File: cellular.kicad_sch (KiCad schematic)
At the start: 37 parts, among them J2 USB_C_Receptacle_USB2.0_14P, J4 SIM_Card_Shielded, J6 Conn_01x04_Pin, Q2 MMBT3904, Q3 MMBT3904, Q4 MMBT3904, SW4 SW_Push, U13 SIM7080G, U19 TPD3F303DPV

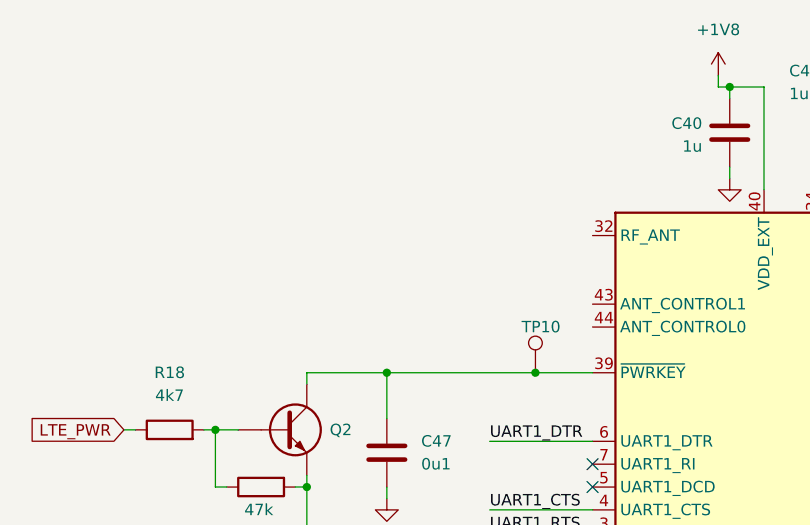
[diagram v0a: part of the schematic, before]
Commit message: schem: add modem lte rf ant
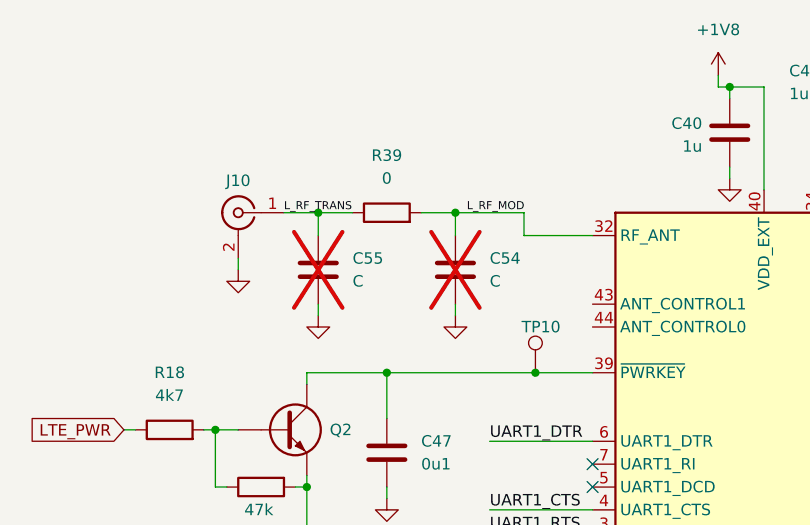
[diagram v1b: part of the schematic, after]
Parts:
- added C54, C55: C, Capacitor_SMD:C_0402_1005Metric, symbol Device:C
- added J10: Conn_Coaxial, Connector_Coaxial:U.FL_Hirose_U.FL-R-SMT-1_Vertical, symbol Connector:Conn_Coaxial
- added R39: 0, symbol Device:R
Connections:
- net GND: now also C54.2, C55.2, J10.2 (Ext)
- net L_RF_MOD: now reaches U13.32 (RF_ANT)
- net L_RF_MOD: now also C54.1, R39.2
- new net L_RF_TRANS: C55.1, J10.1 (In), R39.1

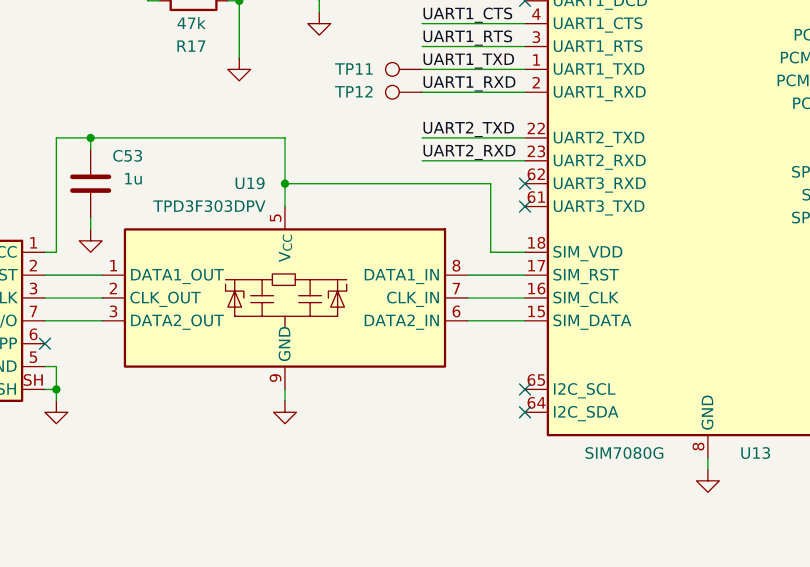
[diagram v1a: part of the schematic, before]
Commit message: schem: add test points
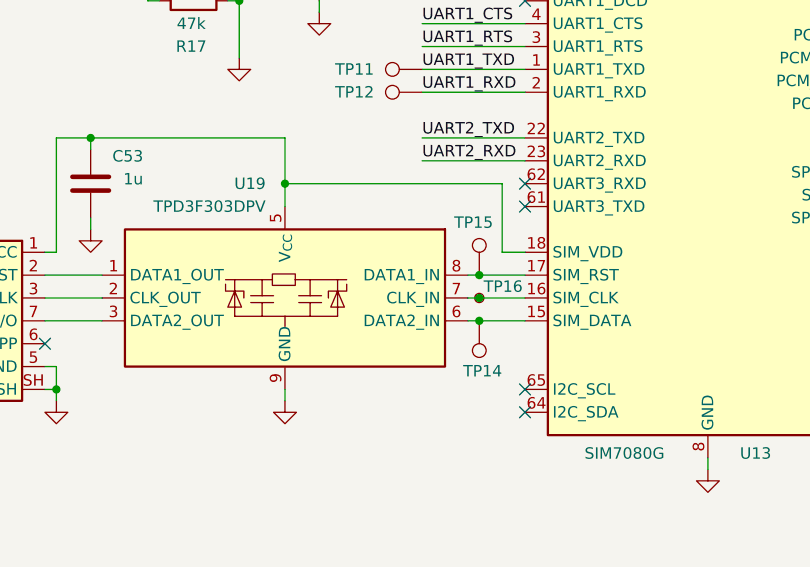
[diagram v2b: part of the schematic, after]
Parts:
- added TP14, TP15: TestPoint, TestPoint:TestPoint_Pad_D2.0mm, symbol Connector:TestPoint
- added TP16: TestPoint, TestPoint:TestPoint_Pad_D2.0mm, symbol Connector:TestPoint_Small
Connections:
- net at U13.15 (SIM_DATA), U19.6 (DATA2_IN): now also TP14.1
- net at U13.16 (SIM_CLK), U19.7 (CLK_IN): now also TP16.1
- net at U13.17 (SIM_RST), U19.8 (DATA1_IN): now also TP15.1

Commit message: schem: run and fix ERC
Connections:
- net D+ renamed MODEM_D+
- net D- renamed MODEM_D-
- no-connect marks 21 -> 24
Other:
- moved on the sheet: SW4

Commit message: schem: add net classes
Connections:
- net L_RF_MOD renamed RF_MOD_L
- net L_RF_TRANS renamed RF_TRANS_L
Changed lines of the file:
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@@
 		)
 	)
-	(label "L_RF_MOD"
+	(label "RF_MOD_L"
 		(at 196.85 38.1 0)
 		(effects
@@
 		)
 	)
-	(label "L_RF_TRANS"
+	(label "RF_TRANS_L"
 		(at 176.53 38.1 0)
 		(effects
@@
 		)
 	)
+	(rule_area
+		(exclude_from_sim no)
+		(in_bom yes)
+		(on_board yes)
+		(dnp no)
+		(polyline
+			(pts
+				(xy 127 91.44) (xy 127 121.285) (xy 207.01 121.285) (xy 207.01 91.44)
+			)
+			(stroke
+				(width 0)
+				(type dash)
+			)
+			(fill
+				(type none)
+			)
+		)
+	)
+	(netclass_flag ""
+		(length 2.54)
+		(shape round)
+		(at 129.54 91.44 0)
+		(fields_autoplaced yes)
+		(effects
+			(font
+				(size 1.27 1.27)
+			)
+			(justify left bottom)
+		)
+		(property "Netclass" "SIM"
+			(at 130.2385 88.9 0)
+			(show_name no)
+			(do_not_autoplace no)
+			(effects
+				(font
+					(size 1.27 1.27)
+				)
+				(justify left)
+			)
+		)
+		(property "Component Class" ""
+			(at -102.87 3.81 0)
+			(show_name no)
+			(do_not_autoplace no)
+			(effects
+				(font
+					(size 1.27 1.27)
+					(italic yes)
+				)
+			)
+		)
+	)
 	(symbol
 		(lib_id "power:GND")
@@
 		(dnp no)
 		(property "Reference" "TP14"
-			(at 208.28 109.728 0)
+			(at 206.502 110.49 0)
 			(show_name no)
 			(do_not_autoplace no)
@@
 		(dnp no)
 		(property "Reference" "U19"
-			(at 182.0067 88.9 0)
+			(at 180.594 110.998 0)
 			(show_name no)
 			(do_not_autoplace no)
@@
 		)
 		(property "Value" "TPD3F303DPV"
-			(at 182.0067 91.44 0)
+			(at 180.594 113.03 0)
 			(show_name no)
 			(do_not_autoplace no)
@@
 		(dnp no)
 		(property "Reference" "TP15"
-			(at 202.946 93.218 0)
+			(at 201.422 92.964 0)
 			(show_name no)
 			(do_not_autoplace no)

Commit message: schem: add footprints
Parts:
- U13: footprint RF_GSM:SIMCom_SIM800C -> GLCS:SIMCom_SIM7080G
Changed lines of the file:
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@@
 			)
 		)
-		(property "Footprint" "RF_GSM:SIMCom_SIM800C"
+		(property "Footprint" "GLCS:SIMCom_SIM7080G"
 			(at 245.11 90.17 0)
 			(hide yes)

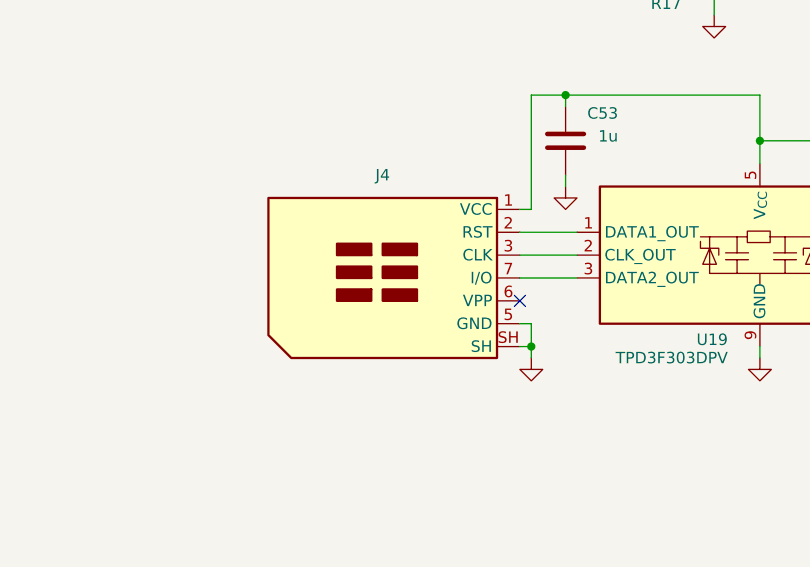
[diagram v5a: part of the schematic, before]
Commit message: schem: add ordering info to BOM
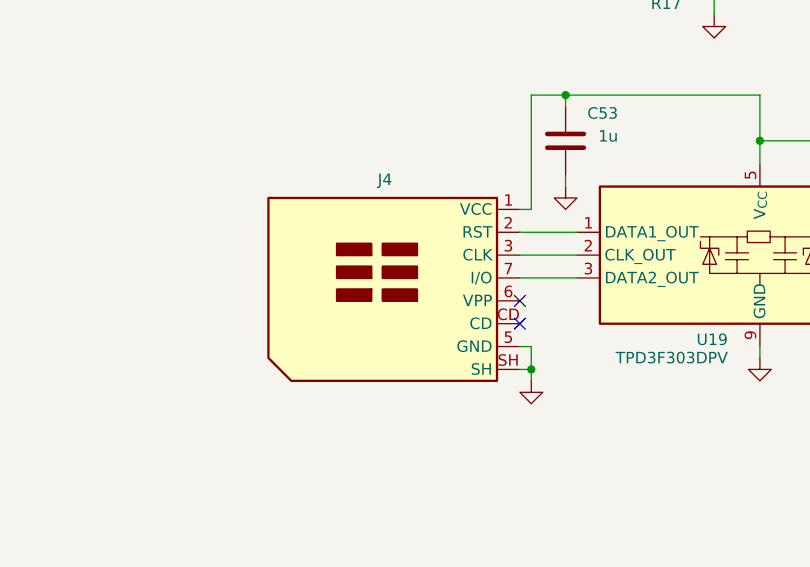
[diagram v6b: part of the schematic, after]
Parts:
- J4: Basic (none) -> X; JLCPCB Part # (none) -> C720512; Manufacturer (none) -> XUNPU; Manufacturer Part Number (none) -> SMN-305-ARP7
- Q2, Q3, Q4: Basic (none) -> Y; JLCPCB Part # (none) -> C20526; Manufacturer (none) -> Jiangsu Changjing Electronics Technology Co., Ltd.; Manufacturer Part Number (none) -> MMBT3904(RANGE:100-300)
- R17, R31, R35: footprint (none) -> Resistor_SMD:R_0402_1005Metric; Basic (none) -> Y; JLCPCB Part # (none) -> C25792; Manufacturer (none) -> Uniroyal Elec; Manufacturer Part Number (none) -> 0402WGF4702TCE
- R18, R19, R34: footprint (none) -> Resistor_SMD:R_0402_1005Metric; Basic (none) -> Y; JLCPCB Part # (none) -> C25900; Manufacturer (none) -> Uniroyal Elec; Manufacturer Part Number (none) -> 0402WGF4701TCE
- R39: footprint (none) -> Resistor_SMD:R_0402_1005Metric; Basic (none) -> Y; JLCPCB Part # (none) -> C17168; Manufacturer (none) -> Uniroyal Elec; Manufacturer Part Number (none) -> 0402WGF0000TCE
- TP16: now left out of the parts list
- U13: Basic (none) -> X; JLCPCB Part # (none) -> C2943992; Manufacturer (none) -> SIMCom Wireless Solutions; Manufacturer Part Number (none) -> C2943992
- U19: Basic (none) -> X; JLCPCB Part # (none) -> C2865991; Manufacturer (none) -> Texas Instruments; Manufacturer Part Number (none) -> TPD3F303DPVR
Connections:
- no-connect marks 24 -> 25

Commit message: schem: add sheet titles
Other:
- company: (none) -> Rémi Ait-Younes
- title: (none) -> S6TM Detect Carrier 2
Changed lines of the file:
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@@
 	(generator_version "10.0")
 	(paper "A4")
+	(title_block
+		(title "S6TM Detect Carrier 2")
+		(date "2026-09-24")
+		(rev "01")
+		(company "Rémi Ait-Younes")
+	)
 	(rectangle
 		(start 48.26 95.25)

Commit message: schem: reannotate
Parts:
- renumbered C53 to C40, C55 to C41, C47 to C42, C54 to C43, C40 to C44, C41 to C45, C42 to C46, C43 to C47, C44 to C48, C45 to C49, C46 to C50, D13 to D10, D14 to D11, D15 to D12, D11 to D13, D12 to D14, J2 to J6, J6 to J7, J4 to J8, J10 to J9, Q3 to Q2, Q4 to Q3, Q2 to Q4, R38 to R28, R33 to R29, R37 to R30, R19 to R31, R31 to R32, R32 to R33, R18 to R37, R17 to R38, TP15 to TP11, TP16 to TP12, TP14 to TP13, TP11 to TP8, TP12 to TP9, U19 to U13, U13 to U14
